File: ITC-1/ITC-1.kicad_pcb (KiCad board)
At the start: 4 copper layers, 82 parts, among them K1 кнопка, K2 кнопка, X1 крепеж, X2 крепеж

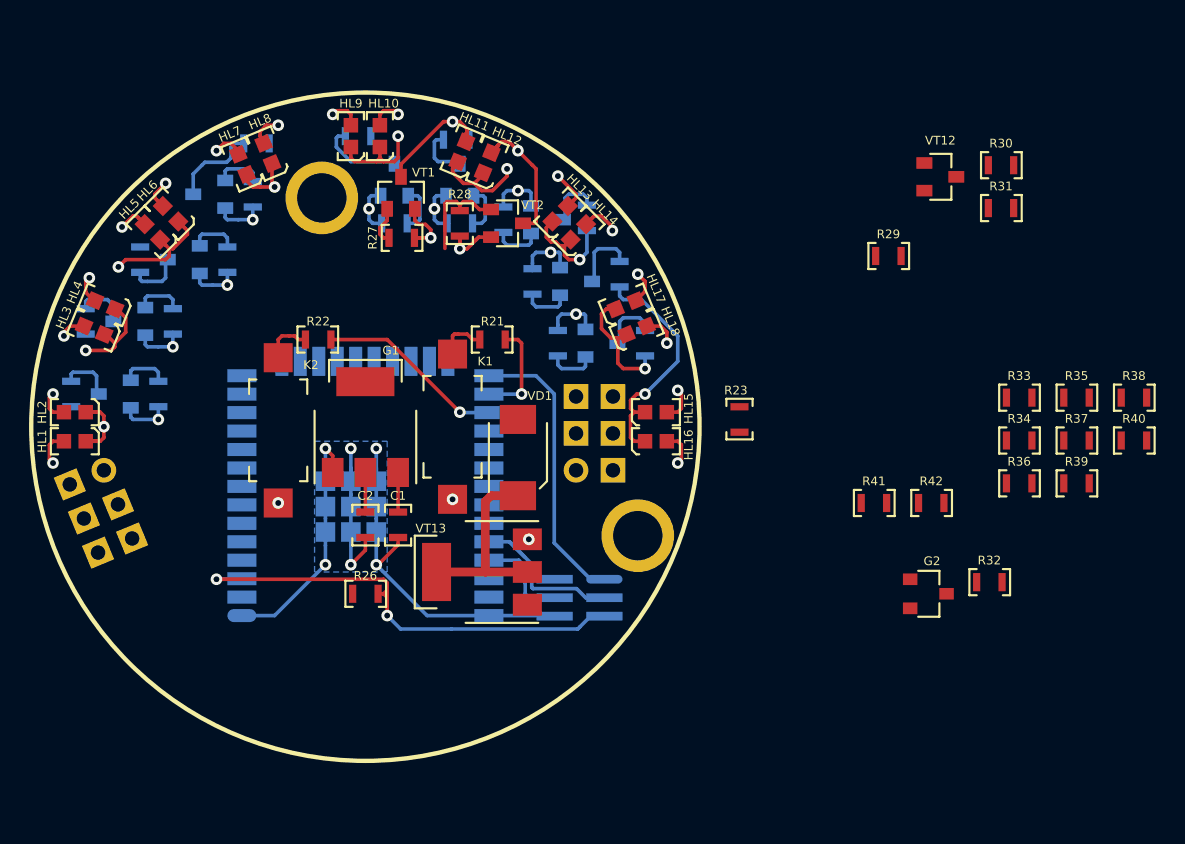
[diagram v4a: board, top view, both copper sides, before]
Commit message: раскинуты все разъемы, требуется подключить LED и поставить лого
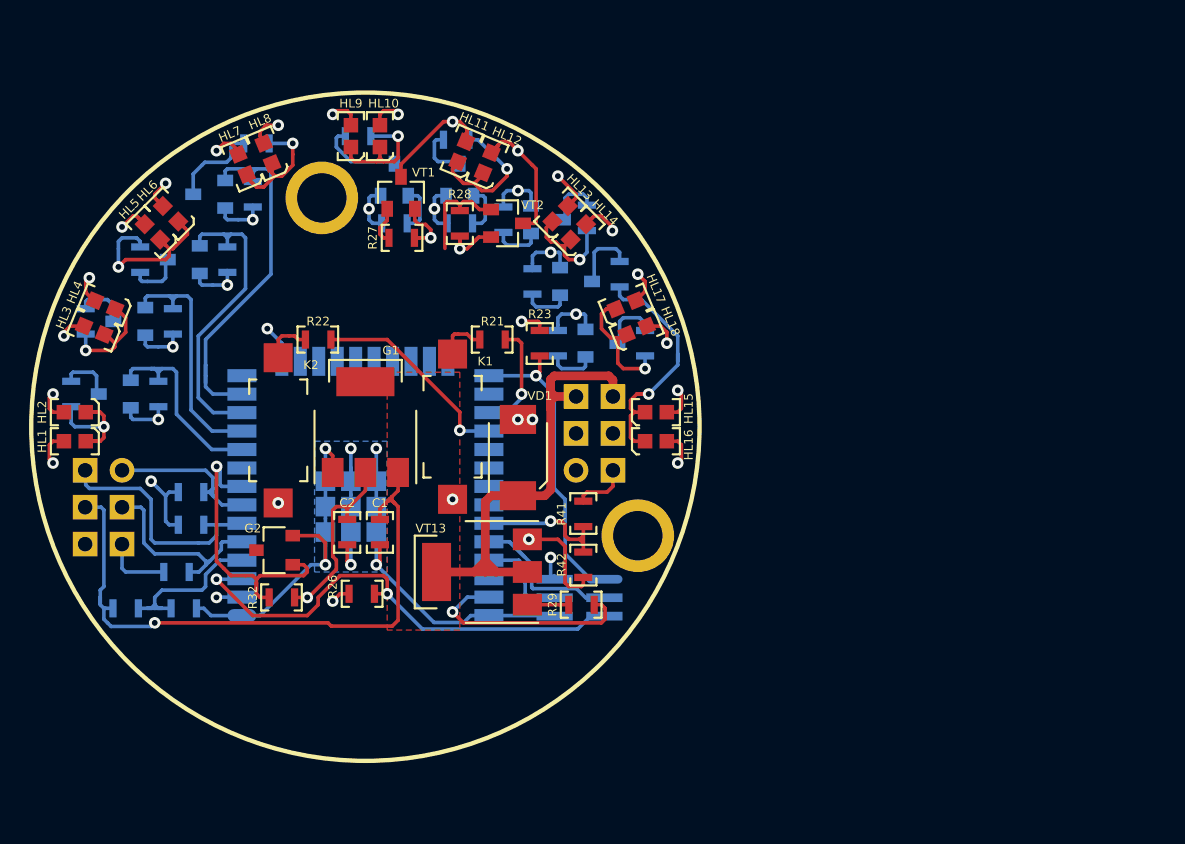
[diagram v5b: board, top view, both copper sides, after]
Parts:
- removed R30, R31, R34, R35, R36: Резистор_0,065Вт, N_RLC:Резистор_SMD_0603_0,065_Вт_pnp
- removed VT12: Транзистор_полевой_N-IRLML6344TR, N_VD_HL:Транзистор_IRLML6344TR_SOT-23
- R33, R37, R38, R39, R40: moved to B.Cu
- moved R38 67.0 mm to (87.0, 85.0), turned to 180 degrees
- moved R40 65.0 mm to (88.0, 79.5), turned to 180 degrees
- moved R33 63.2 mm to (83.5, 87.5), turned to 180 degrees
- moved R37 62.5 mm to (87.5, 87.5)
- moved R39 61.0 mm to (88.0, 81.8), turned to 180 degrees
- moved R32 48.7 mm to (94.2, 86.8), turned to 180 degrees
- moved G2 45.1 mm to (93.8, 83.5), turned to 180 degrees
- moved R29 32.0 mm to (114.9, 87.2), turned to 180 degrees
- moved R42 24.3 mm to (115.0, 84.5), turned to 270 degrees
- moved R41 20.0 mm to (115.0, 81.0), turned to 90 degrees
- moved R23 14.7 mm to (112.0, 69.2), turned to 270 degrees
- moved C1 1.35 mm to (101.0, 82.2)
- moved C2 1.35 mm to (98.8, 82.2)
- moved XP5 1.25 mm to (83.2, 78.0), turned to 270 degrees
- moved R26 0.25 mm to (99.8, 86.5)
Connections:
- A1 pad 10: /LED_2 -> /LED_1
- A1 pad 11: /LED_3 -> /LED_2
- A1 pad 12: /LED_4 -> /LED_3
- A1 pad 13: /LED_5 -> /LED_4
- A1 pad 16: /LED_9 -> /LED_RED
- A1 pad 24: /LED_RED -> /LED_5
- A1 pad 26: /BUTT_1 -> /LED_6
- A1 pad 27: /BUTT_2 -> /BUTT_1
- A1 pad 28: /LED_8 -> /BUTT_2
- A1 pad 30: /LED_6 -> /LED_8
- A1 pad 31: Net-(A1-Pad31) -> /LED_9
- A1 pad 36: /LED-DRIVE -> Net-(A1-Pad36)
- A1 pad 5: /ADC1-CH3 -> /3-LION
- A1 pad 6: /ADC1-CH6 -> /2-LION
- A1 pad 7: /ADC1-CH7 -> /1-LION
- A1 pad 9: /LED_1 -> Net-(A1-Pad9)
- R32 pad 1: /4-LION -> /3V3
- R38 pad 1: /ADC1-CH3 -> /3-LION
- R39 pad 1: /ADC1-CH6 -> /2-LION
- R40 pad 1: /ADC1-CH7 -> /1-LION
- XP5 pad 1: /4-LION -> /1-LION
- XP5 pad 2: /3-LION -> /2-LION
- XP5 pad 3: /2-LION -> /3-LION
- XP5 pad 4: /1-LION -> /4-LION
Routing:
- net /4-LION: track 2.88 -> 99.8 mm, vias 0 -> 3
- net /GND: track 86.9 -> 129.6 mm, vias 18 -> 20
- net /3V3: track 11.0 -> 45.8 mm, vias 2 -> 7
- net /LED_4: track 3.22 -> 25.7 mm
- net /MOTOR-GND: track 13.5 -> 35.4 mm
- net /ADC1-CH4: track 0.00 -> 20.2 mm, vias 0 -> 1
- net /LED_3: track 3.22 -> 20.9 mm
- net /2-LION: track 0.00 -> 16.6 mm
- net /MOTOR-DRIVE: track 0.00 -> 15.4 mm, vias 0 -> 1
- net /3-LION: track 0.00 -> 13.9 mm
- net /LED_2: track 3.22 -> 16.9 mm
- net /ADC1-CH0: track 0.00 -> 11.7 mm
- net /1-LION: track 0.00 -> 10.9 mm
- net /LED_1: track 3.22 -> 13.8 mm
- net /CHARGE-SENS: track 0.00 -> 9.85 mm, vias 0 -> 1
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- added copper zone on In2.Cu-VCC, net /3V3
- added copper zone on In1.Cu-GND, net /GND
- added copper zone on F.Cu, net /MOTOR-GND
- removed copper zone on In2.Cu, net /3V3
- removed copper zone on In1.Cu, net /GND

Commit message: готова трассировка, требуется контрольная проверка
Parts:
- added D1: LOGO, N_ICO:ni_10x10, B.Cu at (94.2, 65.8)
- added D2: LOGO, N_ICO:VLAD_10x10, F.Cu at (100.0, 92.8)
- moved R21 5.59 mm to (103.2, 68.0), turned to 0 degrees
- moved R22 1.00 mm to (96.8, 68.0)
- moved K2 0.25 mm to (94.0, 70.0)
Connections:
- A1 pad 27: /BUTT_1 -> /LED_7
- A1 pad 28: /BUTT_2 -> /LED_8
- A1 pad 29: /LED_7 -> /LED_9
- A1 pad 30: /LED_8 -> /BUTT_1
- A1 pad 31: /LED_9 -> /BUTT_2
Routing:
- net /LED_6: track 3.22 -> 19.1 mm
- net /LED_7: track 3.22 -> 18.7 mm
- net /LED_RED: track 2.56 -> 15.8 mm, vias 0 -> 1
- net /LED_GREEN: track 7.00 -> 20.0 mm, vias 0 -> 1
- net /LED_8: track 3.22 -> 14.9 mm
- net /LED_5: track 3.22 -> 14.1 mm
- net /LED_9: track 3.22 -> 13.5 mm
- net /BUTT_2: track 14.2 -> 22.8 mm
- net /BUTT_1: track 7.69 -> 14.7 mm
- net Net-(K2-Pad1): track 3.33 -> 5.33 mm
- net Net-(K1-Pad1): track 3.33 -> 4.83 mm
- net /4-LION: track 99.8 -> 98.7 mm
- net /BOOT_SEL: track 20.3 -> 21.0 mm, vias 1 -> 2
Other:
- board outline added: 46 x 46 mm

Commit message: добавлено отверстие для бондажа, требуется заменить светодиоды
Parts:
- added X3: крепеж, N_X:ОтверстиеD1.2, F.Cu at (120.0, 78.2)
- added X4: крепеж, N_X:ОтверстиеD1.2, F.Cu at (85.8, 76.2)

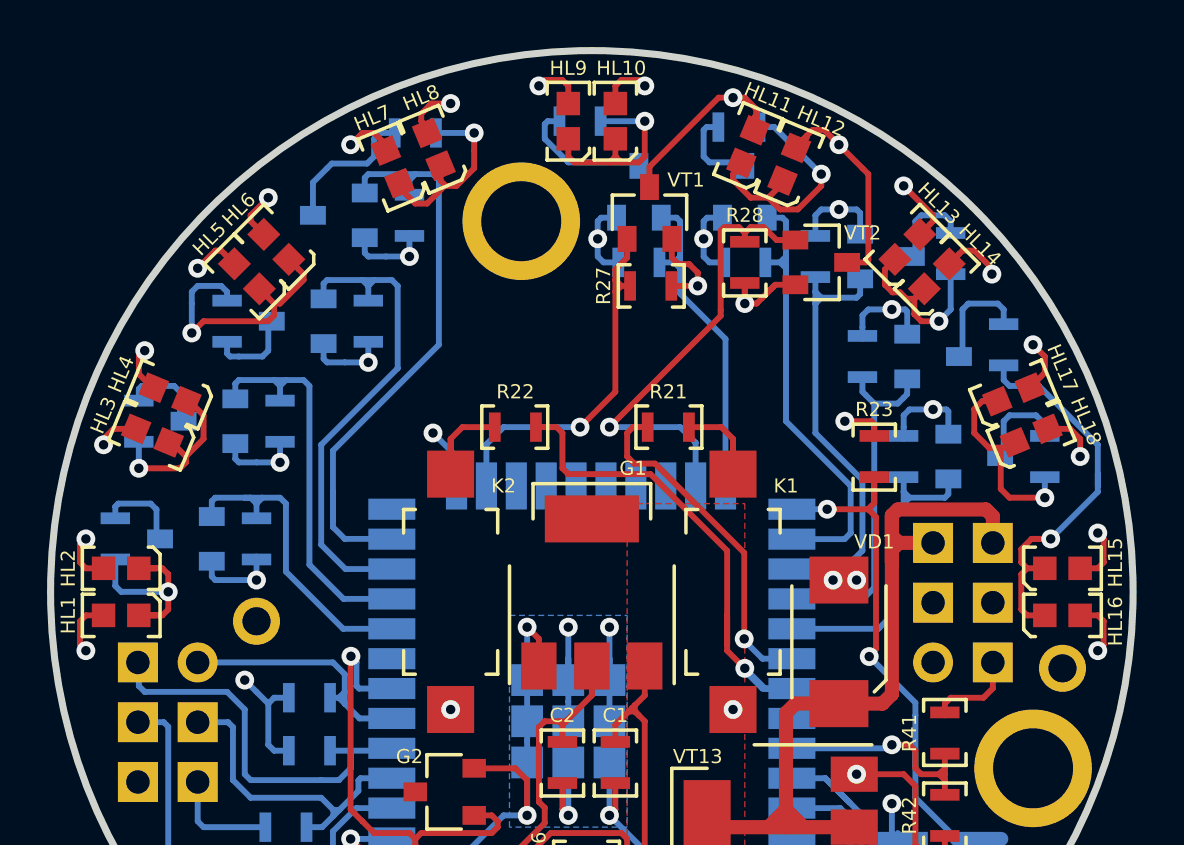
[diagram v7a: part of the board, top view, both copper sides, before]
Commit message: заменены светодиоды на сдвоенные
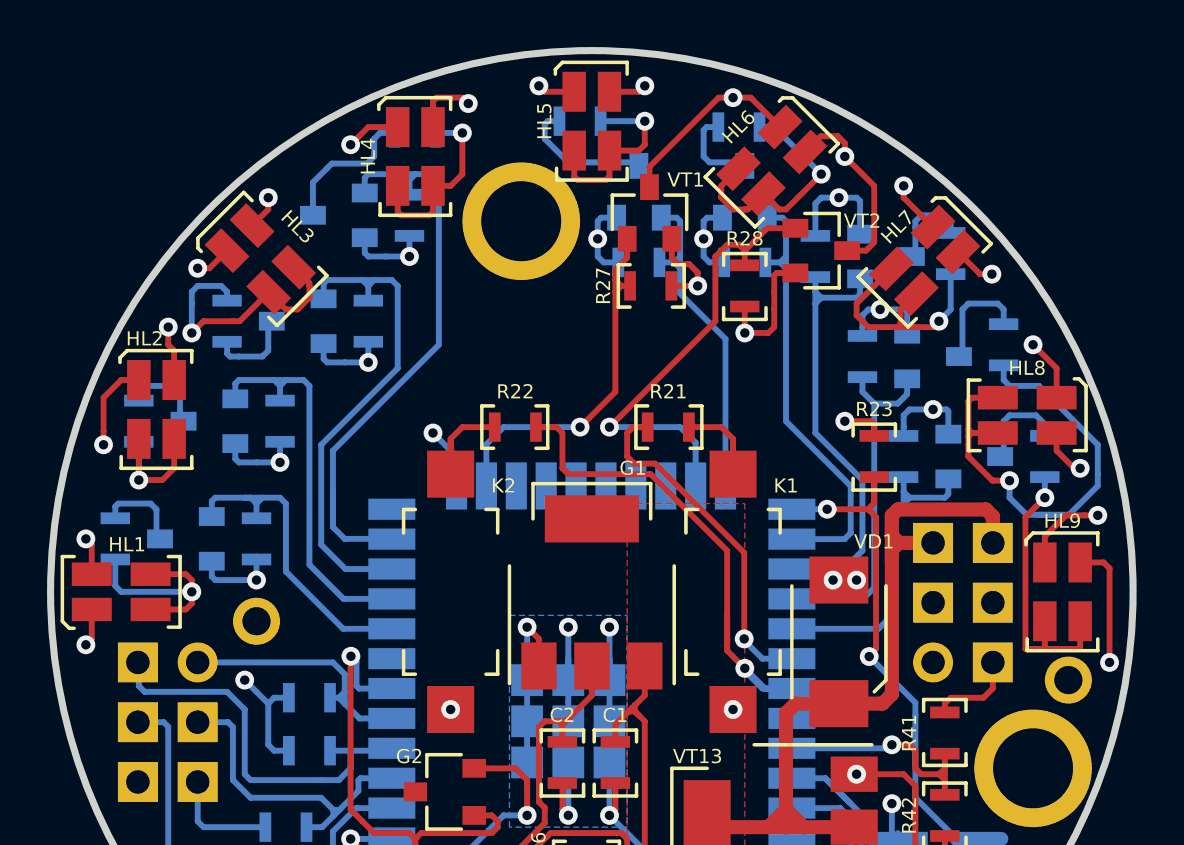
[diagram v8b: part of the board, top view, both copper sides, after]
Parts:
- removed HL10, HL12, HL14, HL16, HL18: ЗЕЛЕНЫЙ, N_VD_HL:Светодиод_SMD_0603
- removed HL11, HL13, HL15, HL17: КРАСНЫЙ, N_VD_HL:Светодиод_SMD_0603
- HL1, HL3, HL5, HL7, HL9: value КРАСНЫЙ -> Светодиод_сдвоенный_KPB-3025SURKCGKC; footprint N_VD_HL:Светодиод_SMD_0603 -> N_VD_HL:Светодиод_SMD_m3025
- HL2, HL4, HL6, HL8: value ЗЕЛЕНЫЙ -> Светодиод_сдвоенный_KPB-3025SURKCGKC; footprint N_VD_HL:Светодиод_SMD_0603 -> N_VD_HL:Светодиод_SMD_m3025
- moved HL8 29.0 mm to (119.8, 66.8), turned to 270 degrees
- moved HL9 28.1 mm to (119.2, 73.8), turned to 0 degrees
- moved HL7 23.5 mm to (114.5, 59.5), turned to 315 degrees
- moved HL6 22.4 mm to (108.0, 55.2)
- moved HL5 16.2 mm to (99.2, 53.8), turned to 0 degrees
- moved HL4 15.2 mm to (91.8, 55.2), turned to 0 degrees
- moved HL3 8.50 mm to (84.5, 60.5), turned to 45 degrees
- moved HL2 8.14 mm to (80.8, 66.0)
- moved R28 1.00 mm to (106.5, 62.0)
- moved HL1 0.56 mm to (78.8, 75.8), turned to 90 degrees
- moved X3 0.56 mm to (120.2, 78.8)
- moved VT2 0.50 mm to (109.8, 60.5)
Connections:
- HL2 pad 1: /3V3-GREEN -> /3V3-RED
- HL2 pad 2: Net-(HL1-Pad2) -> Net-(HL2-Pad2)
- HL4 pad 1: /3V3-GREEN -> /3V3-RED
- HL4 pad 2: Net-(HL3-Pad2) -> Net-(HL4-Pad2)
- HL6 pad 1: /3V3-GREEN -> /3V3-RED
- HL6 pad 2: Net-(HL5-Pad2) -> Net-(HL6-Pad2)
- HL8 pad 1: /3V3-GREEN -> /3V3-RED
- HL8 pad 2: Net-(HL7-Pad2) -> Net-(HL8-Pad2)
- HL9 pad 2: Net-(HL10-Pad2) -> Net-(HL9-Pad2)
- R10 pad 1: Net-(HL5-Pad2) -> Net-(HL3-Pad2)
- R11 pad 1: Net-(HL7-Pad2) -> Net-(HL4-Pad2)
- R12 pad 1: Net-(HL10-Pad2) -> Net-(HL5-Pad2)
- R13 pad 1: Net-(HL11-Pad2) -> Net-(HL6-Pad2)
- R14 pad 1: Net-(HL13-Pad2) -> Net-(HL7-Pad2)
- R17 pad 1: Net-(HL15-Pad2) -> Net-(HL8-Pad2)
- R18 pad 1: Net-(HL17-Pad2) -> Net-(HL9-Pad2)
- R4 pad 1: Net-(HL3-Pad2) -> Net-(HL2-Pad2)
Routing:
- net Net-(HL8-Pad2): track 0.00 -> 20.7 mm, vias 0 -> 1
- net Net-(HL15-Pad2): track 17.7 -> 0.00 mm, vias 1 -> 0
- net Net-(HL9-Pad2): track 0.00 -> 12.3 mm, vias 0 -> 1
- net Net-(HL6-Pad2): track 0.00 -> 10.6 mm, vias 0 -> 1
- net Net-(HL11-Pad2): track 10.2 -> 0.00 mm, vias 1 -> 0
- net Net-(HL10-Pad2): track 9.04 -> 0.00 mm, vias 1 -> 0
- net Net-(HL17-Pad2): track 8.87 -> 0.00 mm, vias 1 -> 0
- net Net-(HL4-Pad2): track 0.00 -> 8.16 mm, vias 0 -> 1
- net Net-(HL13-Pad2): track 7.39 -> 0.00 mm, vias 1 -> 0
- net Net-(HL2-Pad2): track 0.00 -> 6.33 mm, vias 0 -> 1
- net Net-(HL3-Pad2): track 7.22 -> 12.9 mm
- net Net-(HL7-Pad2): track 8.26 -> 10.5 mm
- net /3V3-RED: track 100.4 -> 102.7 mm
- net /3V3-GREEN: track 99.6 -> 101.6 mm
- net /3V3: track 45.8 -> 47.4 mm
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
